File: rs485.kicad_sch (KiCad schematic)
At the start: 6 parts, among them U3 THVD1420D

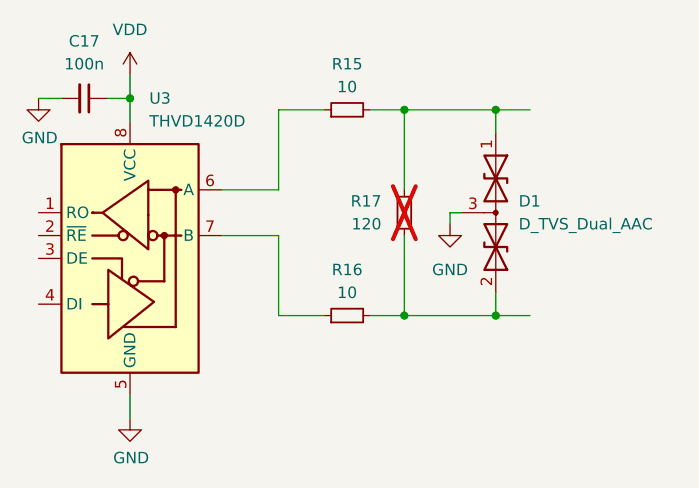
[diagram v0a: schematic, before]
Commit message: Finish rev0 schematics.
Signed-off-by: Dominik Bayerl <dominik.bayerl@carissma.eu>
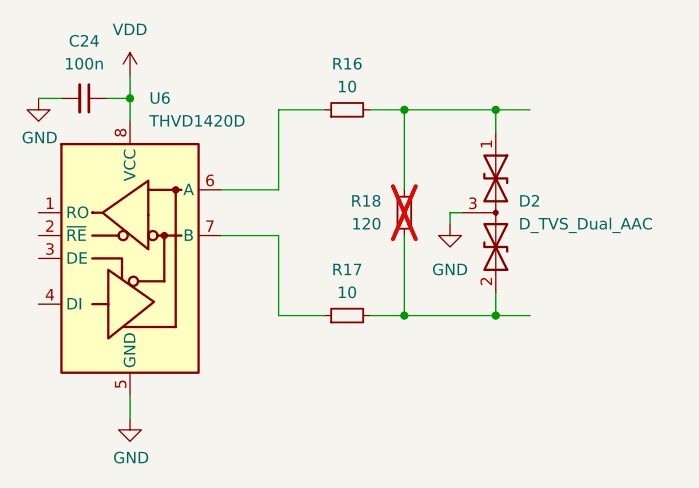
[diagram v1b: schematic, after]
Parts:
- renumbered C17 to C24, D1 to D2, R15 to R16, R16 to R17, R17 to R18, U3 to U6
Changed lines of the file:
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@@
 		(dnp no)
 		(fields_autoplaced yes)
-		(property "Reference" "U3"
+		(property "Reference" "U6"
 			(at 135.4933 82.55 0)
 			(effects
@@
 			(project "esp32s3-rail"
 				(path "/43c3dd73-0dcc-48c9-a061-d039af0cb18f/df982c01-fbe2-4878-8b67-6a103b3ec576"
-					(reference "U3")
+					(reference "U6")
 					(unit 1)
 				)
@@
 		(dnp no)
 		(fields_autoplaced yes)
-		(property "Reference" "D1"
+		(property "Reference" "D2"
 			(at 176.53 93.9799 90)
 			(effects
@@
 			(project "esp32s3-rail"
 				(path "/43c3dd73-0dcc-48c9-a061-d039af0cb18f/df982c01-fbe2-4878-8b67-6a103b3ec576"
-					(reference "D1")
+					(reference "D2")
 					(unit 1)
 				)
@@
 		(dnp no)
 		(fields_autoplaced yes)
-		(property "Reference" "#PWR081"
+		(property "Reference" "#PWR053"
 			(at 168.91 102.87 0)
 			(effects
@@
 			(project "esp32s3-rail"
 				(path "/43c3dd73-0dcc-48c9-a061-d039af0cb18f/df982c01-fbe2-4878-8b67-6a103b3ec576"
-					(reference "#PWR081")
+					(reference "#PWR053")
 					(unit 1)
 				)
@@
 		(dnp no)
 		(fields_autoplaced yes)
-		(property "Reference" "R15"
+		(property "Reference" "R16"
 			(at 157.48 78.74 90)
 			(effects
@@
 			(project "esp32s3-rail"
 				(path "/43c3dd73-0dcc-48c9-a061-d039af0cb18f/df982c01-fbe2-4878-8b67-6a103b3ec576"
-					(reference "R15")
+					(reference "R16")
 					(unit 1)
 				)
@@
 		(dnp no)
 		(fields_autoplaced yes)
-		(property "Reference" "C17"
+		(property "Reference" "C24"
 			(at 128.2636 76.2 90)
 			(effects
@@
 			(project "esp32s3-rail"
 				(path "/43c3dd73-0dcc-48c9-a061-d039af0cb18f/df982c01-fbe2-4878-8b67-6a103b3ec576"
-					(reference "C17")
+					(reference "C24")
 					(unit 1)
 				)
@@
 		(dnp yes)
 		(fields_autoplaced yes)
-		(property "Reference" "R17"
+		(property "Reference" "R18"
 			(at 161.29 93.9799 0)
 			(effects
@@
 			(project "esp32s3-rail"
 				(path "/43c3dd73-0dcc-48c9-a061-d039af0cb18f/df982c01-fbe2-4878-8b67-6a103b3ec576"
-					(reference "R17")
+					(reference "R18")
 					(unit 1)
 				)
@@
 		(dnp no)
 		(fields_autoplaced yes)
-		(property "Reference" "R16"
+		(property "Reference" "R17"
 			(at 157.48 101.6 90)
 			(effects
@@
 			(project "esp32s3-rail"
 				(path "/43c3dd73-0dcc-48c9-a061-d039af0cb18f/df982c01-fbe2-4878-8b67-6a103b3ec576"
-					(reference "R16")
+					(reference "R17")
 					(unit 1)
 				)
@@
 		(on_board yes)
 		(dnp no)
-		(property "Reference" "#PWR051"
+		(property "Reference" "#PWR052"
 			(at 133.35 124.46 0)
 			(effects
@@
 			(project "esp32s3-rail"
 				(path "/43c3dd73-0dcc-48c9-a061-d039af0cb18f/df982c01-fbe2-4878-8b67-6a103b3ec576"
-					(reference "#PWR051")
+					(reference "#PWR052")
 					(unit 1)
 				)
@@
 		(on_board yes)
 		(dnp no)
-		(property "Reference" "#PWR043"
+		(property "Reference" "#PWR050"
 			(at 123.19 88.9 0)
 			(effects
@@
 			(project "esp32s3-rail"
 				(path "/43c3dd73-0dcc-48c9-a061-d039af0cb18f/df982c01-fbe2-4878-8b67-6a103b3ec576"
-					(reference "#PWR043")
+					(reference "#PWR050")
 					(unit 1)
 				)
@@
 		(dnp no)
 		(fields_autoplaced yes)
-		(property "Reference" "#PWR06"
+		(property "Reference" "#PWR051"
 			(at 133.35 83.82 0)
 			(effects
@@
 			(project "esp32s3-rail"
 				(path "/43c3dd73-0dcc-48c9-a061-d039af0cb18f/df982c01-fbe2-4878-8b67-6a103b3ec576"
-					(reference "#PWR06")
-					(unit 1)
-				)
+					(reference "#PWR051")
+					(unit 1)
+				)
